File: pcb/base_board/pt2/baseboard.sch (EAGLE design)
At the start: 40 parts, among them IC1 LD117AS33TR, P1 RPI3NO-CONNECTORS, SW1 324_SW, SW2 324_SW, SW20 324_SW, SW3 324_SW, SW4 324_SW, U5 CH340C

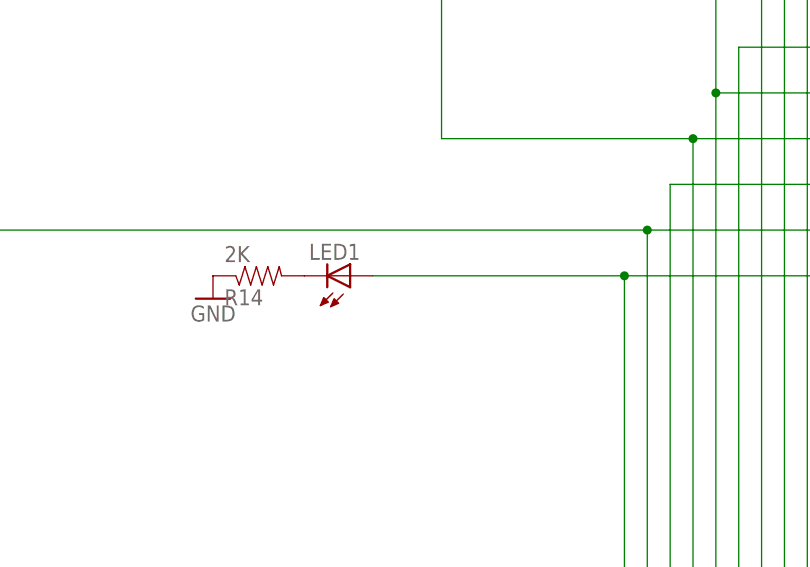
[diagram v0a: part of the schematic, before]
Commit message: added sleep LED on baseboard
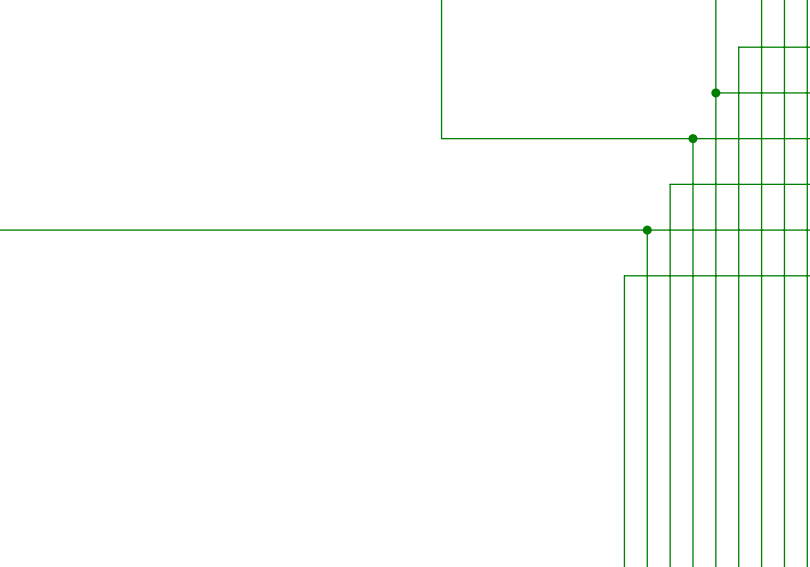
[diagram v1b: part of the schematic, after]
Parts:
- removed LED1: (no value), adafruit:LEDCHIP-LED0805
- removed R14: 2K, SparkFun-Passives:RESISTOR0805-RES
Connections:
- removed net N$10: LED1.C, R14.2
- removed net N$4: LED1.A, P1.GPIO26, P2.37, P3.37
- new net N$21: P1.GPIO26, P2.37, P3.37
- net GND: no longer R14.1
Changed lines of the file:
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@@
 <part name="GND13" library="supply1" library_urn="urn:adsk.eagle:library:371" deviceset="GND" device=""/>
 <part name="JP3" library="adafruit_changed" deviceset="PINHD-1X1" device=""/>
-<part name="LED1" library="adafruit" deviceset="LED" device="CHIP-LED0805"/>
-<part name="R14" library="SparkFun-Passives" deviceset="RESISTOR" device="0805-RES" value="2K"/>
-<part name="GND15" library="backplane" deviceset="GND" device=""/>
 </parts>
 <sheets>
@@
 <attribute name="NAME" x="750.57" y="3.175" size="1.778" layer="95"/>
 <attribute name="VALUE" x="750.57" y="-5.08" size="1.778" layer="96"/>
-</instance>
-<instance part="LED1" gate="G$1" x="543.56" y="5.08" smashed="yes" rot="MR90">
-<attribute name="NAME" x="538.988" y="8.636" size="1.778" layer="95" rot="MR180"/>
-<attribute name="VALUE" x="538.988" y="10.795" size="1.778" layer="96" rot="MR180"/>
-</instance>
-<instance part="R14" gate="G$1" x="533.4" y="5.08" smashed="yes" rot="MR180">
-<attribute name="NAME" x="529.59" y="3.5814" size="1.778" layer="95" rot="MR180"/>
-<attribute name="VALUE" x="529.59" y="8.382" size="1.778" layer="96" rot="MR180"/>
-</instance>
-<instance part="GND15" gate="1" x="528.32" y="2.54" smashed="yes" rot="MR0">
-<attribute name="VALUE" x="530.86" y="0" size="1.778" layer="96" rot="MR0"/>
 </instance>
 </instances>
@@
 <junction x="787.4" y="66.04"/>
 </segment>
-<segment>
-<pinref part="R14" gate="G$1" pin="1"/>
-<pinref part="GND15" gate="1" pin="GND"/>
-</segment>
 </net>
 <net name="+5V" class="0">
@@
 </segment>
 </net>
+<net name="N$21" class="0">
+<segment>
+<pinref part="P2" gate="A" pin="37"/>
+<wire x1="635" y1="-63.5" x2="574.04" y2="-63.5" width="0.1524" layer="91"/>
+<wire x1="574.04" y1="-63.5" x2="574.04" y2="5.08" width="0.1524" layer="91"/>
+<pinref part="P1" gate="G$1" pin="GPIO26"/>
+<wire x1="574.04" y1="5.08" x2="624.84" y2="5.08" width="0.1524" layer="91"/>
+<pinref part="P3" gate="A" pin="37"/>
+<junction x="635" y="-63.5"/>
+</segment>
+</net>
 <net name="N$22" class="0">
 <segment>
@@
 </segment>
 </net>
-<net name="N$10" class="0">
-<segment>
-<pinref part="LED1" gate="G$1" pin="C"/>
-<pinref part="R14" gate="G$1" pin="2"/>
-</segment>
-</net>
-<net name="N$4" class="0">
-<segment>
-<pinref part="LED1" gate="G$1" pin="A"/>
-<pinref part="P2" gate="A" pin="37"/>
-<wire x1="635" y1="-63.5" x2="574.04" y2="-63.5" width="0.1524" layer="91"/>
-<wire x1="574.04" y1="-63.5" x2="574.04" y2="5.08" width="0.1524" layer="91"/>
-<pinref part="P1" gate="G$1" pin="GPIO26"/>
-<wire x1="574.04" y1="5.08" x2="624.84" y2="5.08" width="0.1524" layer="91"/>
-<pinref part="P3" gate="A" pin="37"/>
-<junction x="635" y="-63.5"/>
-<wire x1="546.1" y1="5.08" x2="574.04" y2="5.08" width="0.1524" layer="91"/>
-<junction x="574.04" y="5.08"/>
-</segment>
-</net>
